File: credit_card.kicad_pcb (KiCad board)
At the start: 2 copper layers, 85.6 x 54 mm, 32 parts, among them U1 NT3H2111W0FHKH

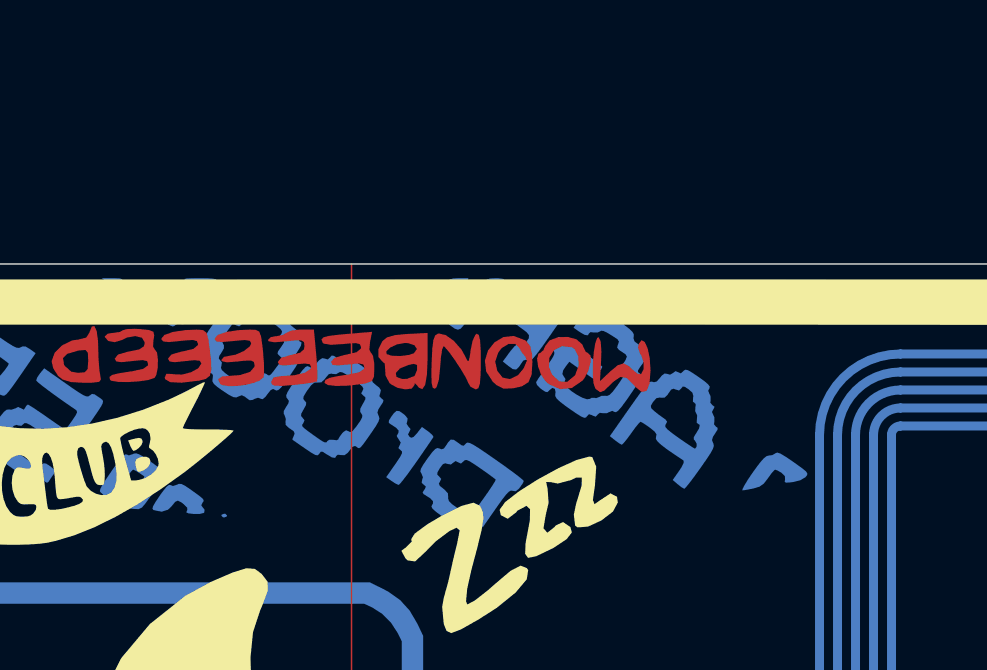
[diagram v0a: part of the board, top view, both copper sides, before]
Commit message: fix nfc antenna issues
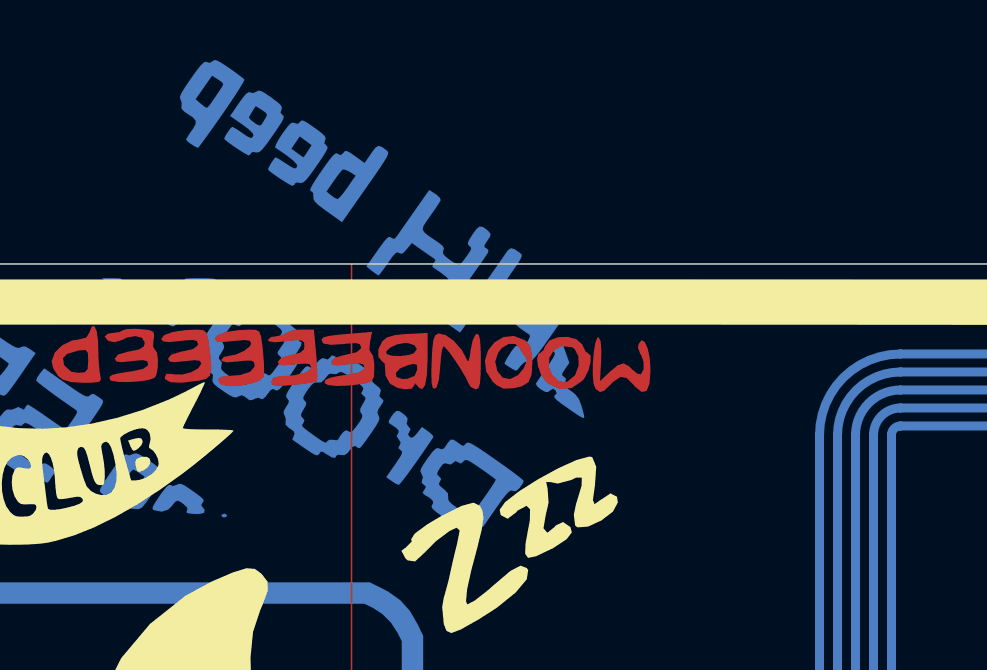
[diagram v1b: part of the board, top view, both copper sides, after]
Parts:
- added G***: LOGO, LOGO, B.Cu at (90.0, 65.4)
- added G***: LOGO, LOGO, B.Cu at (93.2, 59.5)
